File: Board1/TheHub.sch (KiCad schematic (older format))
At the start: 40 parts

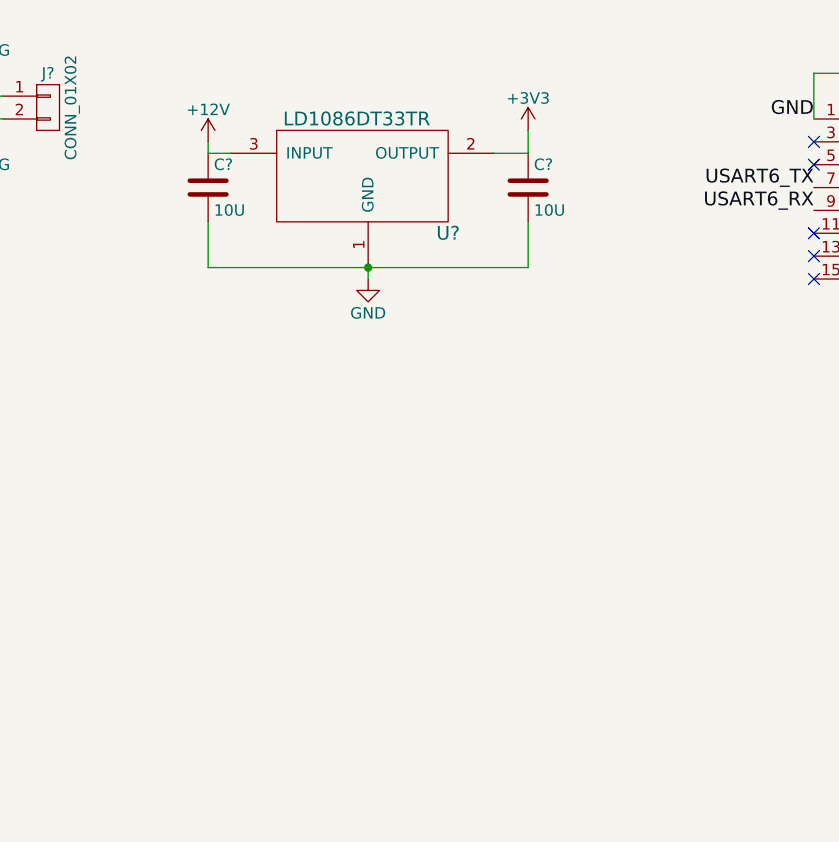
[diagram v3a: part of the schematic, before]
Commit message: Add 5v regulator for RFD900, add power status LEDs fro 5v and 3v3
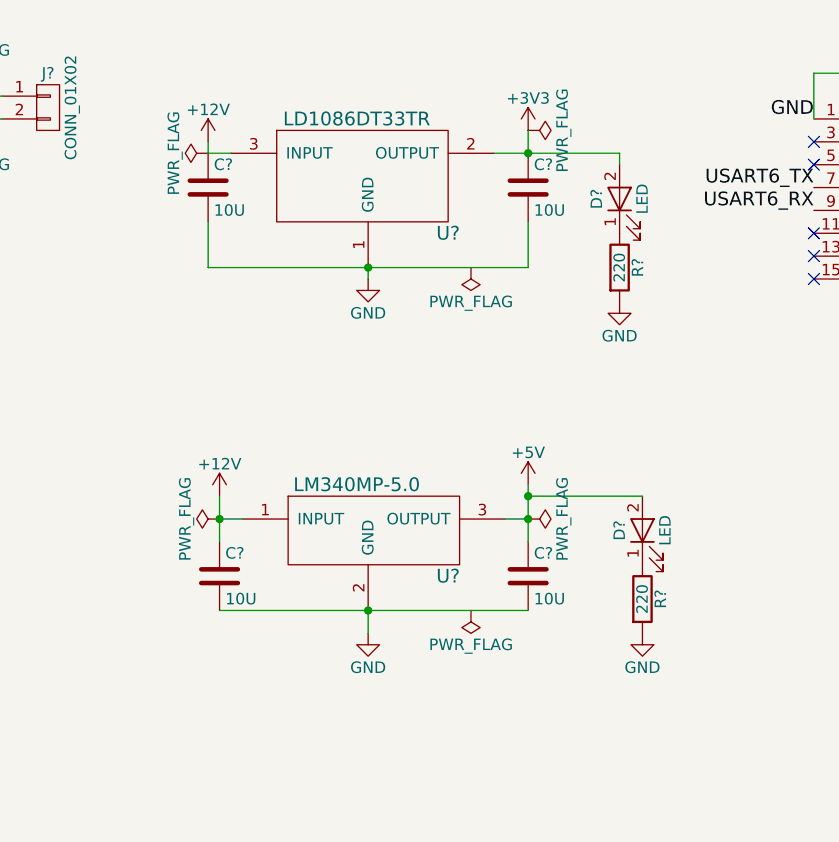
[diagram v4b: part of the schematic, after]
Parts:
- added C? (x2): 10U, symbol C
- added D? (x2): LED, symbol LED
- added R? (x2): 220, symbol R
- added U?: LM340MP-5.0, symbol LM340MP-5.0
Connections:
- net +12V: now also C?.1, U?.1 (INPUT)
- net +3V3: now also D?.2 (A)
- net +5V: now also C?.1, D?.2 (A), U?.3 (OUTPUT)
- net GND: now also C?.2, C?.2, R?.2, R?.2, U?.2 (GND)
- new net: D?.1 (K), R?.1 (x2)
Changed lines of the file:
@@
 	10600 1500 10600 1600
 Wire Wire Line
-	10600 1600 10450 1600
+	10450 1600 11000 1600
 Wire Wire Line
 	7800 1300 7800 1350
@@
 Text Notes 15600 2750 2    60   ~ 0
 With 220Ohm, each led pulls 5mA, for a total of 20mA.
+$Comp
+L LM340MP-5.0 U?
+U 1 1 5937E838
+P 9900 3350
+F 0 "U?" H 10250 3250 60  0000 C CNN
+F 1 "LM340MP-5.0" H 9850 3650 60  0000 C CNN
+F 2 "" H 9900 3350 60  0001 C CNN
+F 3 "" H 9900 3350 60  0001 C CNN
+	1    9900 3350
+	1    0    0    -1
+$EndComp
+$Comp
+L +12V #PWR?
+U 1 1 5937F443
+P 9250 3100
+F 0 "#PWR?" H 9250 2950 50  0001 C CNN
+F 1 "+12V" H 9250 3240 50  0000 C CNN
+F 2 "" H 9250 3100 50  0001 C CNN
+F 3 "" H 9250 3100 50  0001 C CNN
+	1    9250 3100
+	1    0    0    -1
+$EndComp
+$Comp
+L C C?
+U 1 1 593809F4
+P 9250 3450
+F 0 "C?" H 9275 3550 50  0000 L CNN
+F 1 "10U" H 9275 3350 50  0000 L CNN
+F 2 "" H 9288 3300 50  0001 C CNN
+F 3 "" H 9250 3450 50  0001 C CNN
+	1    9250 3450
+	1    0    0    -1
+$EndComp
+$Comp
+L C C?
+U 1 1 59380AB4
+P 10600 3450
+F 0 "C?" H 10625 3550 50  0000 L CNN
+F 1 "10U" H 10625 3350 50  0000 L CNN
+F 2 "" H 10638 3300 50  0001 C CNN
+F 3 "" H 10600 3450 50  0001 C CNN
+	1    10600 3450
+	1    0    0    -1
+$EndComp
+Wire Wire Line
+	9250 3100 9250 3300
+Wire Wire Line
+	9250 3200 9350 3200
+Connection ~ 9250 3200
+$Comp
+L +5V #PWR?
+U 1 1 59380CDB
+P 10600 3050
+F 0 "#PWR?" H 10600 2900 50  0001 C CNN
+F 1 "+5V" H 10600 3190 50  0000 C CNN
+F 2 "" H 10600 3050 50  0001 C CNN
+F 3 "" H 10600 3050 50  0001 C CNN
+	1    10600 3050
+	1    0    0    -1
+$EndComp
+Wire Wire Line
+	10600 3050 10600 3300
+Wire Wire Line
+	10500 3200 10600 3200
+Connection ~ 10600 3200
+Wire Wire Line
+	9250 3600 10600 3600
+Connection ~ 9900 3600
+Wire Wire Line
+	9900 3600 9900 3700
+$Comp
+L GND #PWR?
+U 1 1 59381160
+P 9900 3700
+F 0 "#PWR?" H 9900 3450 50  0001 C CNN
+F 1 "GND" H 9900 3550 50  0000 C CNN
+F 2 "" H 9900 3700 50  0001 C CNN
+F 3 "" H 9900 3700 50  0001 C CNN
+	1    9900 3700
+	1    0    0    -1
+$EndComp
+$Comp
+L PWR_FLAG #FLG?
+U 1 1 593812A1
+P 9250 3200
+F 0 "#FLG?" H 9250 3275 50  0001 C CNN
+F 1 "PWR_FLAG" H 9250 3350 50  0000 C CNN
+F 2 "" H 9250 3200 50  0001 C CNN
+F 3 "" H 9250 3200 50  0001 C CNN
+	1    9250 3200
+	0    -1   -1   0
+$EndComp
+$Comp
+L PWR_FLAG #FLG?
+U 1 1 59381334
+P 9200 1600
+F 0 "#FLG?" H 9200 1675 50  0001 C CNN
+F 1 "PWR_FLAG" H 9200 1750 50  0000 C CNN
+F 2 "" H 9200 1600 50  0001 C CNN
+F 3 "" H 9200 1600 50  0001 C CNN
+	1    9200 1600
+	0    -1   -1   0
+$EndComp
+$Comp
+L PWR_FLAG #FLG?
+U 1 1 59381518
+P 10600 1500
+F 0 "#FLG?" H 10600 1575 50  0001 C CNN
+F 1 "PWR_FLAG" H 10600 1650 50  0000 C CNN
+F 2 "" H 10600 1500 50  0001 C CNN
+F 3 "" H 10600 1500 50  0001 C CNN
+	1    10600 1500
+	0    1    1    0
+$EndComp
+$Comp
+L PWR_FLAG #FLG?
+U 1 1 59381757
+P 10600 3200
+F 0 "#FLG?" H 10600 3275 50  0001 C CNN
+F 1 "PWR_FLAG" H 10600 3350 50  0000 C CNN
+F 2 "" H 10600 3200 50  0001 C CNN
+F 3 "" H 10600 3200 50  0001 C CNN
+	1    10600 3200
+	0    1    1    0
+$EndComp
+$Comp
+L PWR_FLAG #FLG?
+U 1 1 593817E3
+P 10350 2100
+F 0 "#FLG?" H 10350 2175 50  0001 C CNN
+F 1 "PWR_FLAG" H 10350 2250 50  0000 C CNN
+F 2 "" H 10350 2100 50  0001 C CNN
+F 3 "" H 10350 2100 50  0001 C CNN
+	1    10350 2100
+	-1   0    0    1
+$EndComp
+$Comp
+L PWR_FLAG #FLG?
+U 1 1 5938199C
+P 10350 3600
+F 0 "#FLG?" H 10350 3675 50  0001 C CNN
+F 1 "PWR_FLAG" H 10350 3750 50  0000 C CNN
+F 2 "" H 10350 3600 50  0001 C CNN
+F 3 "" H 10350 3600 50  0001 C CNN
+	1    10350 3600
+	-1   0    0    1
+$EndComp
+$Comp
+L R R?
+U 1 1 59383560
+P 11000 2100
+F 0 "R?" V 11080 2100 50  0000 C CNN
+F 1 "220" V 11000 2100 50  0000 C CNN
+F 2 "" V 10930 2100 50  0001 C CNN
+F 3 "" H 11000 2100 50  0001 C CNN
+	1    11000 2100
+	1    0    0    -1
+$EndComp
+$Comp
+L LED D?
+U 1 1 59383605
+P 11000 1800
+F 0 "D?" H 11000 1900 50  0000 C CNN
+F 1 "LED" H 11000 1700 50  0000 C CNN
+F 2 "" H 11000 1800 50  0001 C CNN
+F 3 "" H 11000 1800 50  0001 C CNN
+	1    11000 1800
+	0    -1   -1   0
+$EndComp
+$Comp
+L R R?
+U 1 1 593837E3
+P 11100 3550
+F 0 "R?" V 11180 3550 50  0000 C CNN
+F 1 "220" V 11100 3550 50  0000 C CNN
+F 2 "" V 11030 3550 50  0001 C CNN
+F 3 "" H 11100 3550 50  0001 C CNN
+	1    11100 3550
+	1    0    0    -1
+$EndComp
+$Comp
+L LED D?
+U 1 1 593837E9
+P 11100 3250
+F 0 "D?" H 11100 3350 50  0000 C CNN
+F 1 "LED" H 11100 3150 50  0000 C CNN
+F 2 "" H 11100 3250 50  0001 C CNN
+F 3 "" H 11100 3250 50  0001 C CNN
+	1    11100 3250
+	0    -1   -1   0
+$EndComp
+Wire Wire Line
+	11000 1600 11000 1650
+Connection ~ 10600 1600
+Wire Wire Line
+	10600 3100 11100 3100
+Connection ~ 10600 3100
+$Comp
+L GND #PWR?
+U 1 1 59383C45
+P 11000 2250
+F 0 "#PWR?" H 11000 2000 50  0001 C CNN
+F 1 "GND" H 11000 2100 50  0000 C CNN
+F 2 "" H 11000 2250 50  0001 C CNN
+F 3 "" H 11000 2250 50  0001 C CNN
+	1    11000 2250
+	1    0    0    -1
+$EndComp
+$Comp
+L GND #PWR?
+U 1 1 59383CE4
+P 11100 3700
+F 0 "#PWR?" H 11100 3450 50  0001 C CNN
+F 1 "GND" H 11100 3550 50  0000 C CNN
+F 2 "" H 11100 3700 50  0001 C CNN
+F 3 "" H 11100 3700 50  0001 C CNN
+	1    11100 3700
+	1    0    0    -1
+$EndComp
 $EndSCHEMATC

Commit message: Add additional inputs to autonomy section
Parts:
- removed J?: Morpho Left, symbol CONN_02X19
- removed J?: Morpho Right, symbol CONN_02X19
- removed J?: ARM_ADC_1, symbol CONN_01X04
- removed J?: ARM_ADC_2, symbol CONN_01X04
- added D?: LED, symbol LED
- added J1: ARM_ADC_1, symbol CONN_02X04
- added J2: ARM_ADC_2, symbol CONN_02X04
- added J4: CONN_02X16, symbol CONN_02X16
- added J5: NucleoF411RE, symbol NucleoF411RE
- added J?: GPS, symbol CONN_01X09
- added J?: ANALOG SENSORS, symbol CONN_02X05
- added R?: R, symbol R
- gave numbers to parts that had none: 43
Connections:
- net +3V3: now also J5.16 (P16), J?.8 (P8)
- net +5V: now also J5.18 (P18)
- net A0: now also J?.2 (P2)
- net A1: now also J?.4 (P4)
- net A2: now also J?.6 (P6)
- net A3: now also J?.8 (P8)
- net A4: now also J5.31 (P31), J?.10 (P10)
- net A5: now also J5.25 (P25)
- net AGND: now also J5.32 (P32)
- net AVDD: now also J5.7 (P7)
- net BOOT0: now also J5.7 (P7)
- net D13: now also D?.2 (A)
- net E5V: now also J5.6 (P6)
- net GND: now also J1.2 (P2), J1.4 (P4), J1.6 (P6), J1.8 (P8), J2.2 (P2), J2.4 (P4), J2.6 (P6), J2.8 (P8), J5.19 (P19), J5.20 (P20), J5.20 (P20), J5.22 (P22), J5.8 (P8), J5.9 (P9), J?.1 (P1), J?.3 (P3), J?.5 (P5), J?.7 (P7), J?.7 (P7), J?.9 (P9), R?.1
- net IOREF: now also J5.12 (P12)
- net PA0: now also J5.28 (P28)
- net PA1: now also J5.30 (P30)
- net PA10: now also J5.33 (P33)
- net PA11: now also J5.14 (P14)
- net PA12: now also J5.12 (P12)
- net PA13: now also J5.13 (P13)
- net PA14: now also J5.15 (P15)
- net PA15: now also J5.17 (P17)
- net PA2: now also J5.35 (P35)
- net PA3: now also J5.37 (P37)
- net PA4: now also J5.32 (P32)
- net PA5: now also J5.11 (P11)
- net PA6: now also J5.13 (P13)
- net PA7: now also J5.15 (P15)
- net PA8: now also J5.23 (P23)
- net PA9: now also J5.21 (P21)
- net PB0: now also J5.34 (P34)
- net PB1: now also J5.24 (P24)
- net PB12: now also J5.16 (P16)
- net PB13: now also J5.30 (P30)
- net PB14: now also J5.28 (P28)
- net PB15: now also J5.26 (P26)
- net PB2: now also J5.22 (P22)
- net PB4: now also J5.27 (P27)
- net PB5: now also J5.29 (P29)
- net PB6: now also J5.17 (P17)
- net PB7: now also J5.21 (P21)
- net PB8: now also J5.3 (P3)
- net PB9: now also J5.5 (P5)
- net PC0: now also J5.38 (P38)
- net PC1: now also J5.36 (P36)
- net PC10: now also J5.1 (P1)
- net PC11: now also J5.2 (P2)
- net PC12: now also J5.3 (P3)
- net PC13: now also J5.23 (P23)
- net PC14: now also J5.25 (P25)
- net PC15: now also J5.27 (P27)
- net PC2: now also J5.35 (P35)
- net PC3: now also J5.37 (P37)
- net PC4: now also J5.34 (P34)
- net PC5: now also J5.6 (P6)
- net PC6: now also J5.4 (P4)
- net PC7: now also J5.19 (P19)
- net PC8: now also J5.2 (P2)
- net PC9: now also J5.1 (P1)
- net PD2: now also J5.4 (P4)
- net PH0: now also J5.29 (P29)
- net PH1: now also J5.31 (P31)
- net RESET: now also J5.14 (P14)
- net RX0: now also J?.5 (P5)
- net TX1: now also J?.6 (P6)
- net U5V: now also J5.8 (P8)
- net VBAT: now also J5.33 (P33)
- net VDD: now also J5.5 (P5)
- net at U2.10 (A3): now also J1.7 (P7)
- net at U2.7 (A0): now also J1.1 (P1)
- net at U2.8 (A1): now also J1.3 (P3)
- net at U2.9 (A2): now also J1.5 (P5)
- net at U3.10 (A3): now also J2.7 (P7)
- net at U3.7 (A0): now also J2.1 (P1)
- net at U3.8 (A1): now also J2.3 (P3)
- net at U3.9 (A2): now also J2.5 (P5)
- new net: D?.1 (K), R?.2
- no-connect marks 29 -> 58

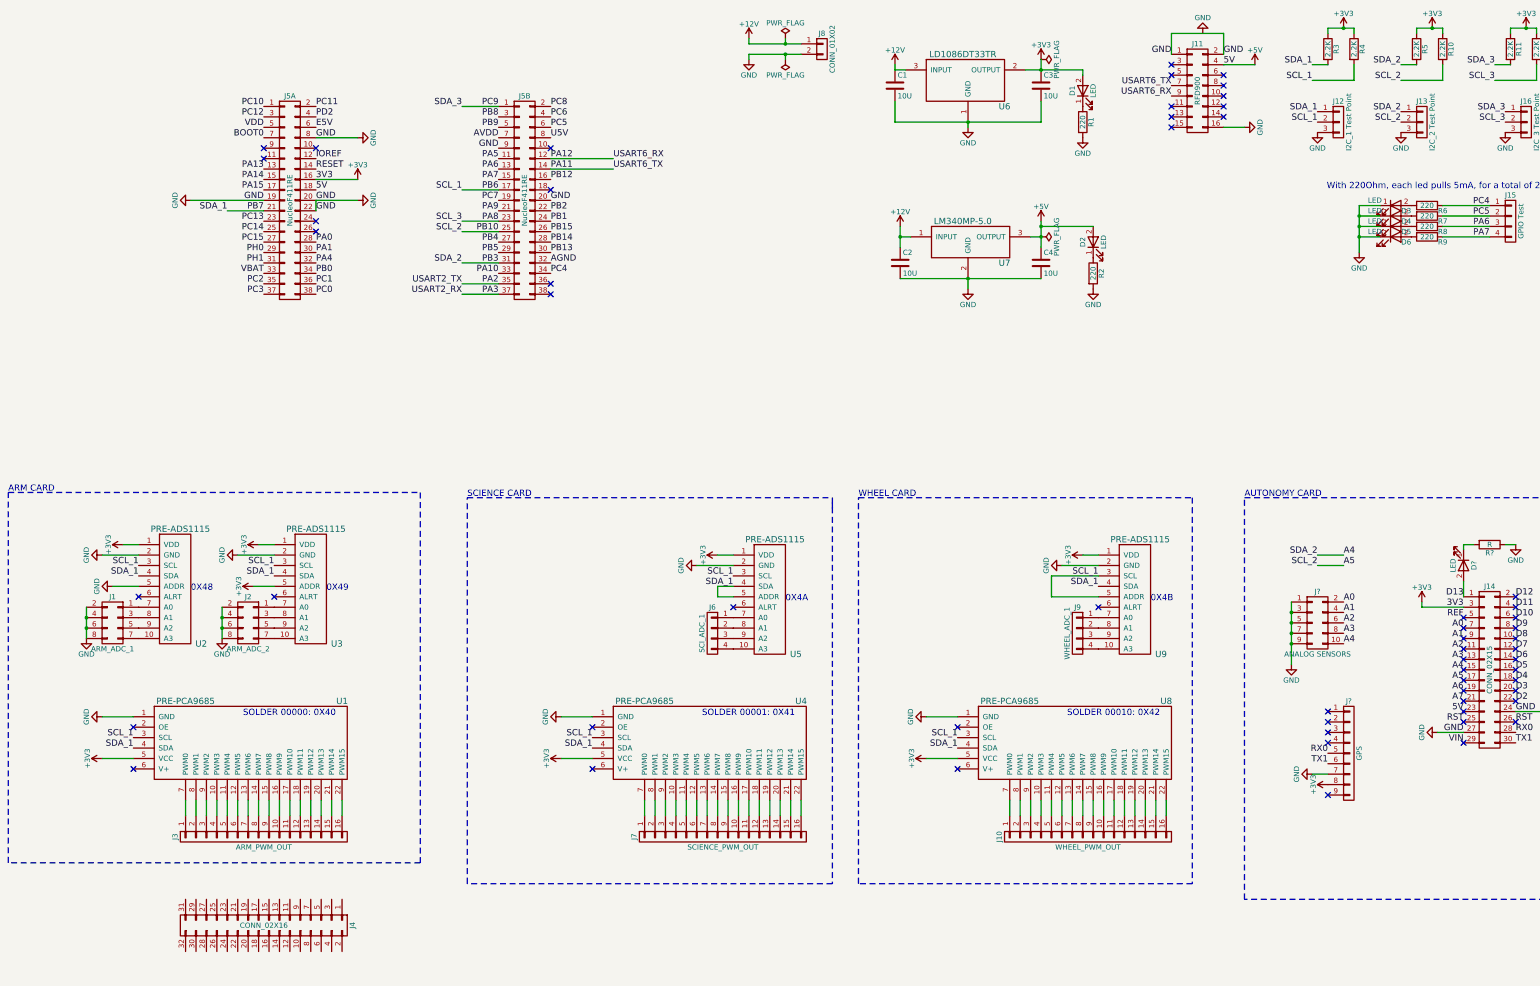
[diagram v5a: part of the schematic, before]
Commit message: Add option for second external regulated voltage, add connections for servo power on wheels, science, and arm cards
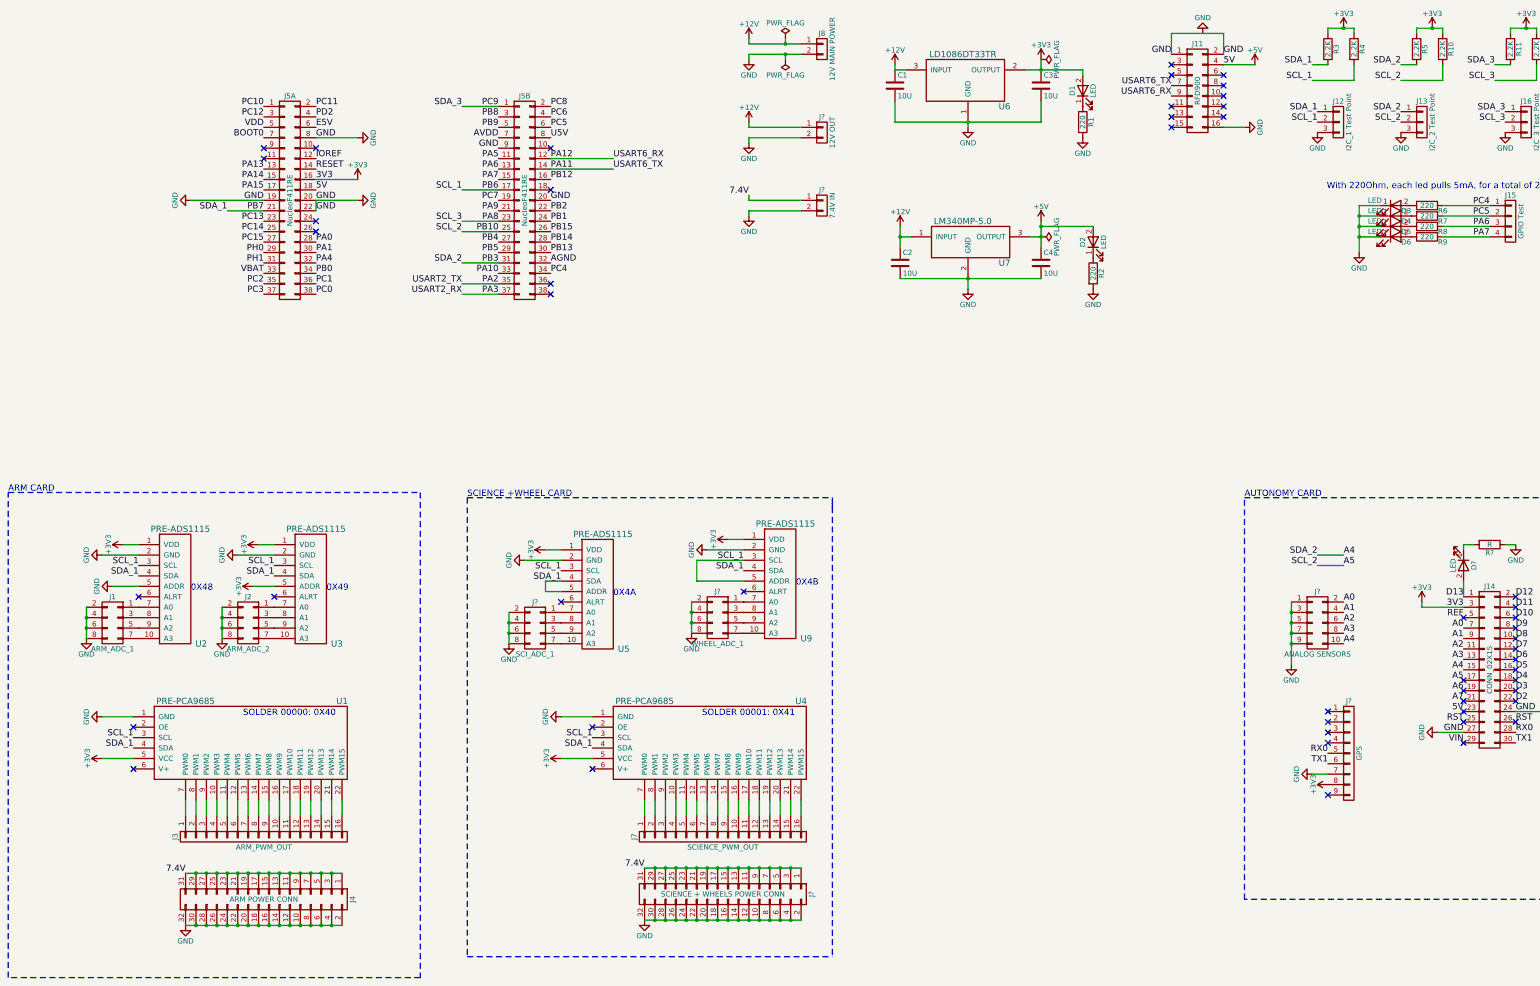
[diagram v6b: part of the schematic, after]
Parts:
- removed J10: WHEEL_PWM_OUT, symbol CONN_01X16
- removed J6: SCI_ADC_1, symbol CONN_01X04
- removed J9: WHEEL_ADC_1, symbol CONN_01X04
- removed U8: PRE-PCA9685, symbol PRE-PCA9685
- added J?: SCI_ADC_1, symbol CONN_02X04
- added J?: WHEEL_ADC_1, symbol CONN_02X04
- added J?: 12V OUT, symbol CONN_01X02
- added J?: 7.4V IN, symbol CONN_01X02
- added J?: SCIENCE + WHEELS POWER CONN, symbol CONN_02X16
- J4: value CONN_02X16 -> ARM POWER CONN
- J8: value CONN_01X02 -> 12V MAIN POWER
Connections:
- net +12V: now also J?.1 (P1)
- net GND: now also J4.10 (P10), J4.12 (P12), J4.14 (P14), J4.16 (P16), J4.18 (P18), J4.2 (P2), J4.20 (P20), J4.22 (P22), J4.24 (P24), J4.26 (P26), J4.28 (P28), J4.30 (P30), J4.32 (P32), J4.4 (P4), J4.6 (P6), J4.8 (P8), J?.10 (P10), J?.12 (P12), J?.14 (P14), J?.16 (P16), J?.18 (P18), J?.2 (P2), J?.2 (P2), J?.2 (P2), J?.2 (P2), J?.2 (P2), J?.20 (P20), J?.22 (P22), J?.24 (P24), J?.26 (P26), J?.28 (P28), J?.30 (P30), J?.32 (P32), J?.4 (P4), J?.4 (P4), J?.4 (P4), J?.6 (P6), J?.6 (P6), J?.6 (P6), J?.8 (P8), J?.8 (P8), J?.8 (P8)
- net at U9.10 (A3): now also J?.7 (P7)
- net at U9.7 (A0): now also J?.1 (P1)
- net at U9.8 (A1): now also J?.3 (P3)
- net at U9.9 (A2): now also J?.5 (P5)
- net at U5.10 (A3): now also J?.7 (P7)
- net at U5.7 (A0): now also J?.1 (P1)
- net at U5.8 (A1): now also J?.3 (P3)
- net at U5.9 (A2): now also J?.5 (P5)
- net 7.4V: now reaches J4.1 (P1)
- net 7.4V: now also J4.11 (P11), J4.13 (P13), J4.15 (P15), J4.17 (P17), J4.19 (P19), J4.21 (P21), J4.23 (P23), J4.25 (P25), J4.27 (P27), J4.29 (P29), J4.3 (P3), J4.31 (P31), J4.5 (P5), J4.7 (P7), J4.9 (P9), J?.1 (P1), J?.1 (P1), J?.11 (P11), J?.13 (P13), J?.15 (P15), J?.17 (P17), J?.19 (P19), J?.21 (P21), J?.23 (P23), J?.25 (P25), J?.27 (P27), J?.29 (P29), J?.3 (P3), J?.31 (P31), J?.5 (P5), J?.7 (P7), J?.9 (P9)
- no-connect marks 58 -> 51
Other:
- note added: "SCIENCE +WHEEL CARD"
- note removed: "SCIENCE CARD"
- note removed: "SOLDER 00010: 0X42"
- note removed: "WHEEL CARD"
- moved on the sheet: J4, U5, U9

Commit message: Add support for compass on I2C_2, provide prodcut specific guidlines for sensor compatibility
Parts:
- added J21: COMPASS, symbol CONN_01X06
- gave numbers to parts that had none: 9
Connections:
- net +3V3: now also J21.6 (P6)
- net +5V: no longer J14.23 (P23)
- net A4: now also J21.3 (P3)
- net A5: now also J21.2 (P2)
- net GND: now also J21.5 (P5)
- net RST: no longer names the net of J14.25 (P25)
- net RST: no longer J14.26 (P26)
- no-connect marks 51 -> 52
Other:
- note added: "USE ADAFRUIT HMC5883L\nFOR COMPATIBILITY"
- note added: "USE ADAFRUIT ULTIMATE GPS\nFOR COMPATIBILITY"
- moved on the sheet: J1, J10, J2, J3, J4, J6, J7, J9, U1, U2, U3, U4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
